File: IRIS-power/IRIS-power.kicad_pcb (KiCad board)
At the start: 2 copper layers, 66.9 x 65 mm, 83 parts, among them J11 Powerpole, J12 PJ-047AH, J13 IRIS_power_board, Q21 2N7002, Q61 IRLML6402, U11 TVS1400DRV, U12 TVS1400DRV, U21 MAX17261, U31 TPS2121, U41 TPS55340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

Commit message: Begin revising for IRIS V4
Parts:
- J13: value IRIS_power_board -> Conn_01x20_MountingPin; footprint star-common-lib:IRIS_Power_Physical -> star-common-lib:IRIS_Muons_physical
- moved C21 33.4 mm to (13.8, 18.5)
- moved C22 33.4 mm to (12.5, 10.8)
- moved C31 33.4 mm to (60.8, -5.75)
- moved C32 33.4 mm to (60.8, 5.75)
- moved C33 33.4 mm to (57.8, 3.75)
- moved C34 33.4 mm to (55.2, 1.75)
- moved C35 33.4 mm to (57.8, -3.75)
- moved C61 33.4 mm to (29.2, -28.2)
- moved C62 33.4 mm to (29.2, -19.8)
- moved C63 33.4 mm to (22.0, -26.5)
- moved D31 33.4 mm to (52.5, 0.00)
- moved J11 33.4 mm to (20.2, 16.5)
- moved J12 33.4 mm to (59.2, -20.5)
- moved Q21 33.4 mm to (10.0, 22.8)
- moved Q61 33.4 mm to (29.0, -9.75)
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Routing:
- net /5V Backup/SCL: track 30.7 -> 3.92 mm, vias 2 -> 1
- net /5V Backup/+5V: track 33.5 -> 10.9 mm
- net /Edge Connector/FB_HV_P: track 26.2 -> 5.01 mm
- net /Edge Connector/FB_HV_N: track 25.7 -> 7.88 mm
- net /5V Backup/SDA: track 30.8 -> 13.5 mm, vias 3 -> 2
- net /3V Supply/+3.3V: track 35.4 -> 24.1 mm, vias 2 -> 1
- net /5V Backup/~CHRG: track 27.6 -> 18.6 mm
- net /5V Backup/~INT: track 7.71 -> 0.00 mm
- net /HV Supply/AGND: track 29.8 -> 28.9 mm
- net GND: vias 163 -> 128
- removed copper zone on F.Cu, net /3V Supply/+3.3V
- removed copper zone on F.Cu, net /3V Supply/VSYS
- removed copper zone on F.Cu, net /5V Supply/+MUX
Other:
- board size 66.9 x 65 mm -> 65 x 65 mm

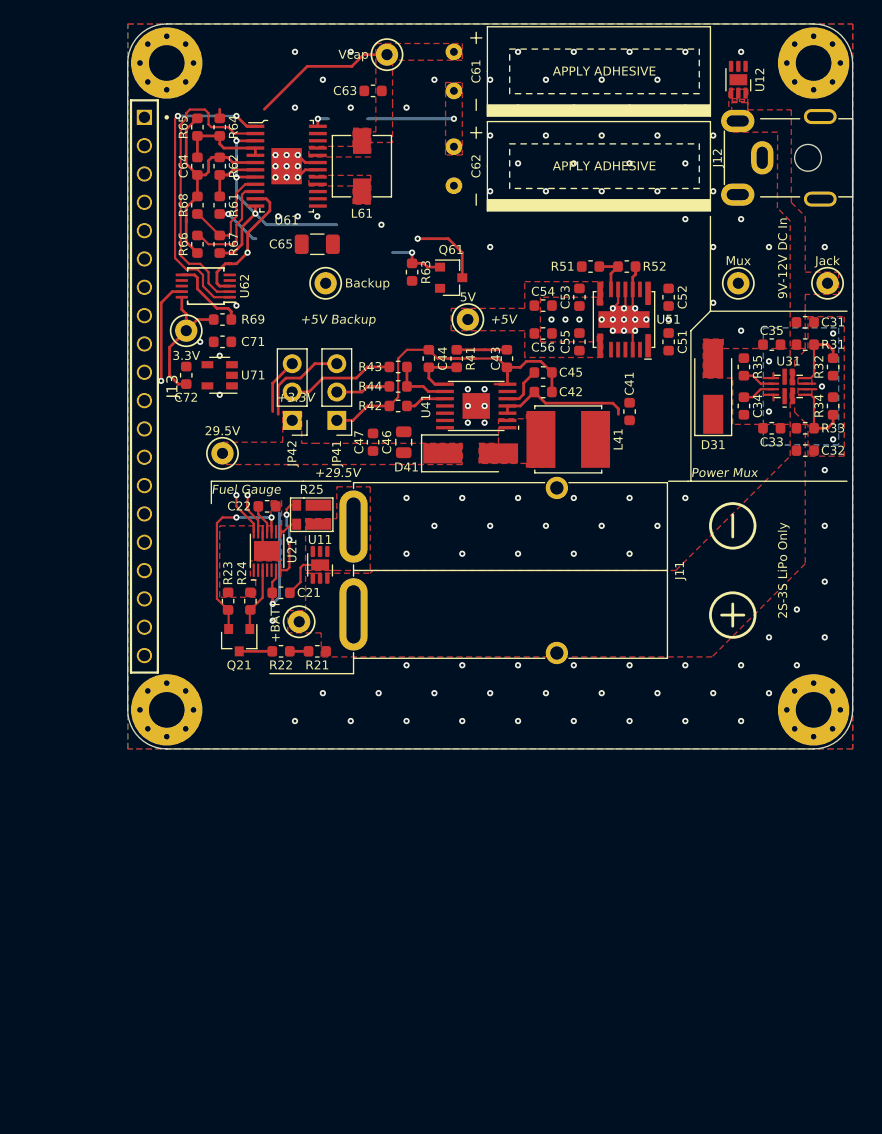
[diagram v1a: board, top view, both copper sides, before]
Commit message: Updated IRIS power board for V4
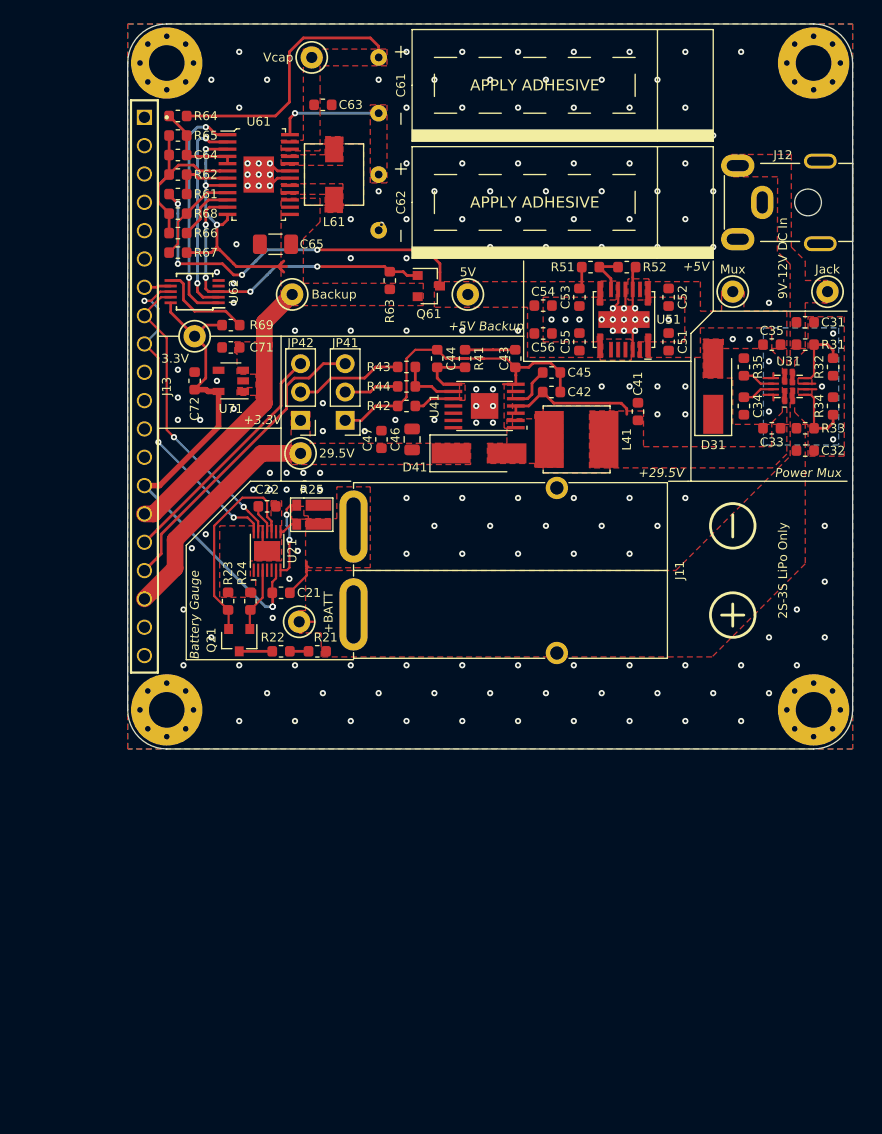
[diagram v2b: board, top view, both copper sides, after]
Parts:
- removed U11, U12: TVS1400DRV, star-common-lib:WSON-6-1EP_2x2mm_Hand_Solder
- C61, C62: footprint star-common-lib:SCCR20B335PRB -> star-common-lib:CAP_10x27_5mm_pitch
- moved C62 7.49 mm to (22.5, -16.5)
- moved TP105 7.00 mm to (15.5, 6.00)
- moved C61 6.86 mm to (22.5, -27.0)
- moved TP61 6.75 mm to (16.5, -29.5)
- moved C63 4.67 mm to (17.5, -25.2), turned to 0 degrees
- moved J12 4.00 mm to (59.2, -16.5)
- moved R61 3.88 mm to (4.50, -17.2), turned to 0 degrees
- moved R64 3.88 mm to (4.50, -24.2), turned to 0 degrees
- moved R62 3.82 mm to (4.50, -19.0), turned to 180 degrees
- moved R67 3.82 mm to (4.50, -12.0), turned to 180 degrees
- moved C65 3.75 mm to (13.2, -12.8)
- moved TP106 3.16 mm to (14.8, -8.25)
- moved L61 2.61 mm to (18.5, -19.0)
- moved NT61 2.61 mm to (7.78, -19.3)
- moved U61 2.61 mm to (11.8, -19.0)
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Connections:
- J13 pad 3: /5V Backup/~INT -> Net-(J13-Pad3)
- J13 pad 7: Net-(J13-Pad7) -> /5V Backup/~INT
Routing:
- net /3V Supply/VSYS: track 24.6 -> 52.2 mm, vias 4 -> 3
- net /5V Backup/SCL: track 3.92 -> 29.6 mm, vias 1 -> 3
- net /5V Backup/+5V: track 10.9 -> 35.9 mm, vias 2 -> 4
- net /3V Supply/+3.3V: track 24.1 -> 46.1 mm, vias 1 -> 2
- net /Edge Connector/+29.5V: track 0.00 -> 20.9 mm
- net /Edge Connector/FB_HV_N: track 7.88 -> 27.2 mm
- net /Edge Connector/FB_HV_P: track 5.01 -> 21.8 mm
- net /5V Backup/SDA: track 13.5 -> 26.7 mm
- net /5V Backup/~CHRG: track 18.6 -> 30.0 mm, vias 2 -> 4
- net /5V Backup/Vcap: track 13.8 -> 24.1 mm
- net /5V Backup/CAP_OK: track 31.4 -> 21.3 mm
- net /5V Backup/~CMP_OUT: track 27.1 -> 18.5 mm, vias 0 -> 2
- net GNDS: track 19.0 -> 14.8 mm
- net /5V Backup/PROG: track 9.65 -> 5.50 mm
- net /5V Backup/~INT: track 0.00 -> 2.40 mm
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- added copper zone on F.Cu, net /3V Supply/VSYS
- added copper zone on F.Cu, net /5V Supply/+MUX
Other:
- board text added: "Battery Gauge"
- board text removed: "Fuel Gauge"

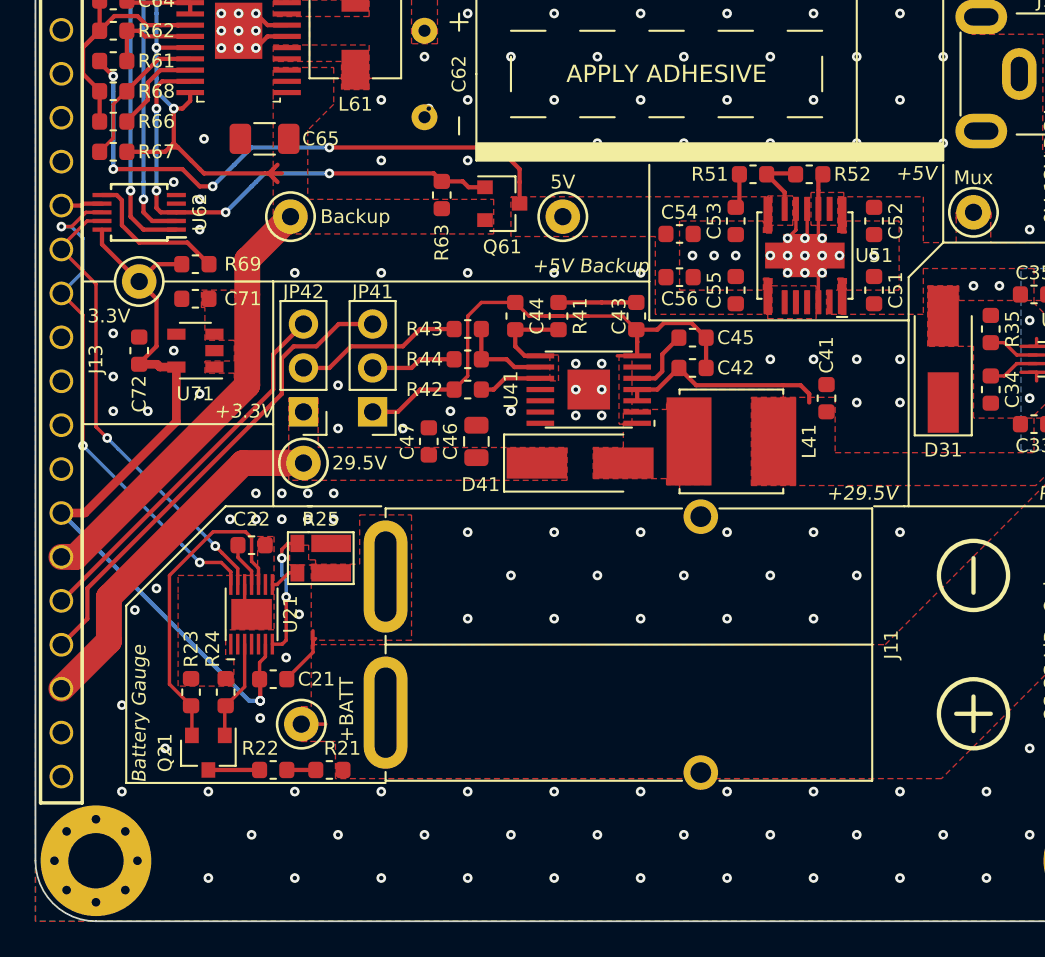
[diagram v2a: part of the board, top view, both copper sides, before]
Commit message: Improved fuel gauge layout
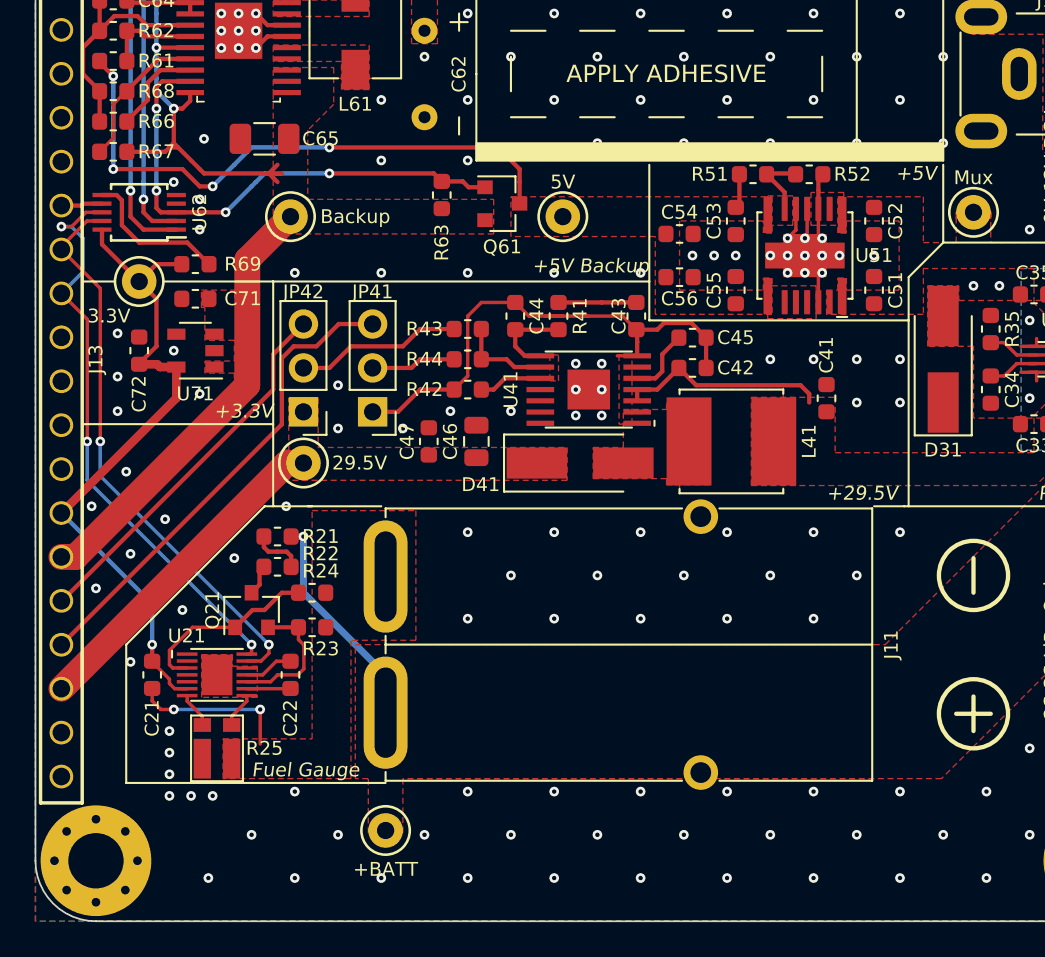
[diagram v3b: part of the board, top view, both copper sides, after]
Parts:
- moved R21 13.8 mm to (14.0, 10.2)
- moved R25 12.5 mm to (10.5, 22.5), turned to 180 degrees
- moved R22 11.8 mm to (14.0, 12.0)
- moved Q21 8.62 mm to (12.5, 14.5), turned to 90 degrees
- moved R23 7.94 mm to (16.0, 15.5), turned to 0 degrees
- moved TP103 7.85 mm to (20.2, 27.2)
- moved C22 7.83 mm to (14.8, 18.2), turned to 270 degrees
- moved R24 7.62 mm to (16.0, 13.5), turned to 0 degrees
- moved C21 7.00 mm to (6.75, 18.2), turned to 270 degrees
- moved U21 4.03 mm to (10.5, 18.2), turned to 0 degrees
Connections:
- R23 pad 2: GND1 -> /Fuel Gauge/-BATT
- R24 pad 2: GND1 -> /Fuel Gauge/-BATT
- R25 pad 1: GND -> /Fuel Gauge/-BATT
- R25 pad 2: /Fuel Gauge/CSN -> GND1
- R25 pad 3: GND1 -> /Fuel Gauge/CSN
- R25 pad 4: /Fuel Gauge/-BATT -> GND
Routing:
- net /Fuel Gauge/+BATT: track 1.43 -> 12.9 mm, vias 0 -> 1
- net /Fuel Gauge/CELLX: track 18.6 -> 7.90 mm
- net /3V Supply/+3.3V: track 46.1 -> 39.4 mm, vias 2 -> 1
- net /5V Backup/SDA: track 26.7 -> 32.9 mm
- net /Fuel Gauge/-BATT: track 3.84 -> 9.17 mm, vias 0 -> 2
- net /Fuel Gauge/CSN: track 7.29 -> 2.06 mm, vias 2 -> 0
- net /Fuel Gauge/SW: track 5.75 -> 10.8 mm
- net /5V Backup/SCL: track 29.6 -> 33.6 mm
- net /Edge Connector/+29.5V: track 20.9 -> 19.4 mm
- net Net-(R21-Pad2): track 1.67 -> 3.02 mm
- net Net-(Q21-Pad3): track 2.96 -> 1.69 mm
- net GND1: track 3.62 -> 4.59 mm
- net GND: vias 185 -> 179
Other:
- board text added: "Fuel Gauge"
- board text removed: "Battery Gauge"

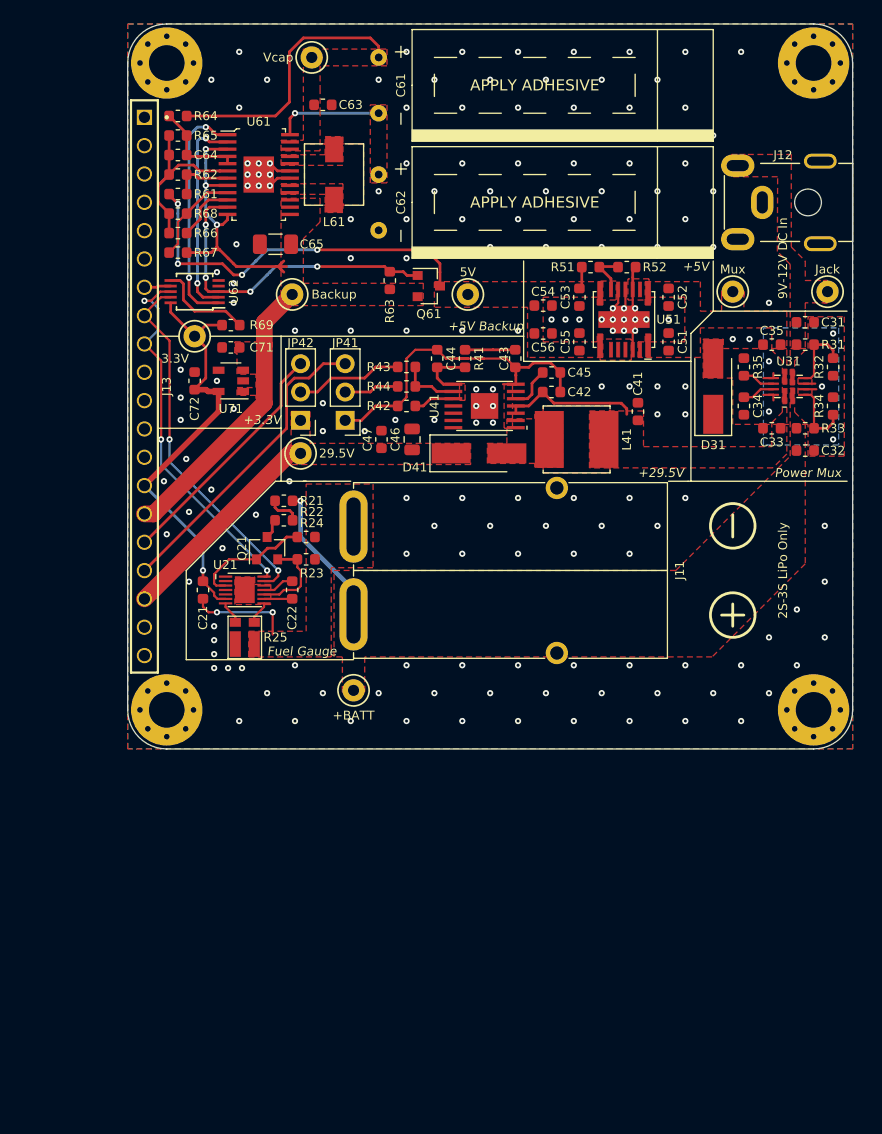
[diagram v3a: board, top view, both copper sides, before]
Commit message: Adjusted silkscreen
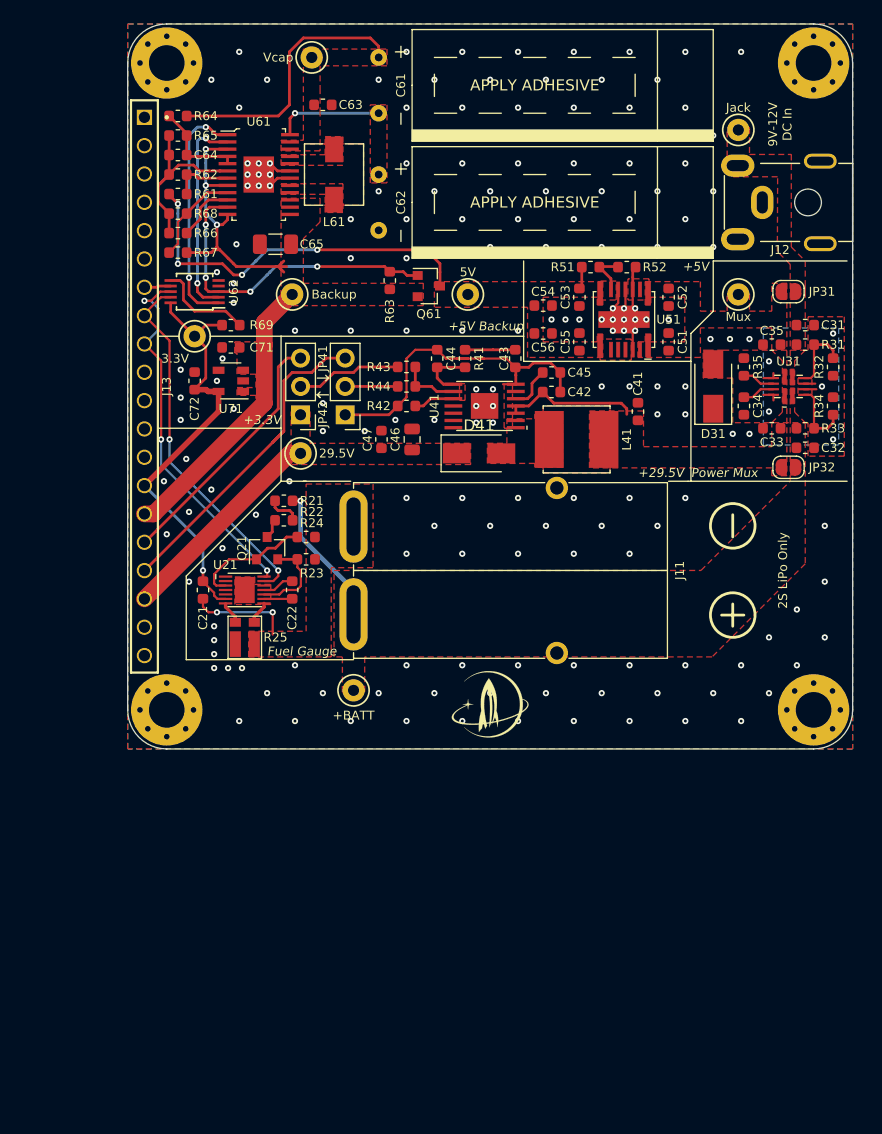
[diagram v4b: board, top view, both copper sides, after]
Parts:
- added G***: LOGO, star-common-lib:star_7x6, F.Cu at (32.5, 28.5)
- added JP31: DC Jack Bypass, Jumper:SolderJumper-2_P1.3mm_Open_RoundedPad1.0x1.5mm, F.Cu at (59.2, -8.50)
- added JP32: Battery Bypass, Jumper:SolderJumper-2_P1.3mm_Open_RoundedPad1.0x1.5mm, F.Cu at (59.2, 7.25)
- D31, D41: footprint Diode_SMD:D_SMA_Handsoldering -> Diode_SMD:D_SMA
- Q61: value IRLML6402 -> DMP2066LSN-7
- R64: value 3570k -> 3.3M
- R65: value 1150k -> 1M
- moved TP101 16.6 mm to (54.8, -23.0)
- moved TP102 0.56 mm to (54.8, -8.25)
- moved JP41 0.50 mm to (19.5, 2.54)
- moved JP42 0.50 mm to (15.5, 2.54)
- moved C31 0.25 mm to (60.8, -5.50)
- moved C32 0.25 mm to (60.8, 5.50)
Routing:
- net /Edge Connector/FB_HV_N: track 27.2 -> 29.9 mm
- net /Edge Connector/FB_HV_P: track 21.8 -> 23.0 mm
- net GND: vias 179 -> 182
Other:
- board text added: "2S LiPo Only"
- board text removed: "2S-3S LiPo Only"
